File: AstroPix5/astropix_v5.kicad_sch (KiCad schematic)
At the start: 40 parts, among them J1 HBOut, J12 Measures_Analog, J14 Bias, J2 Conn_01x05, J3 pcie_GECCO, J4 HBOut, J5 HBOut, J7 HV_in_external, J8 Conn_01x03, U2 AstroPix5_split_powerring

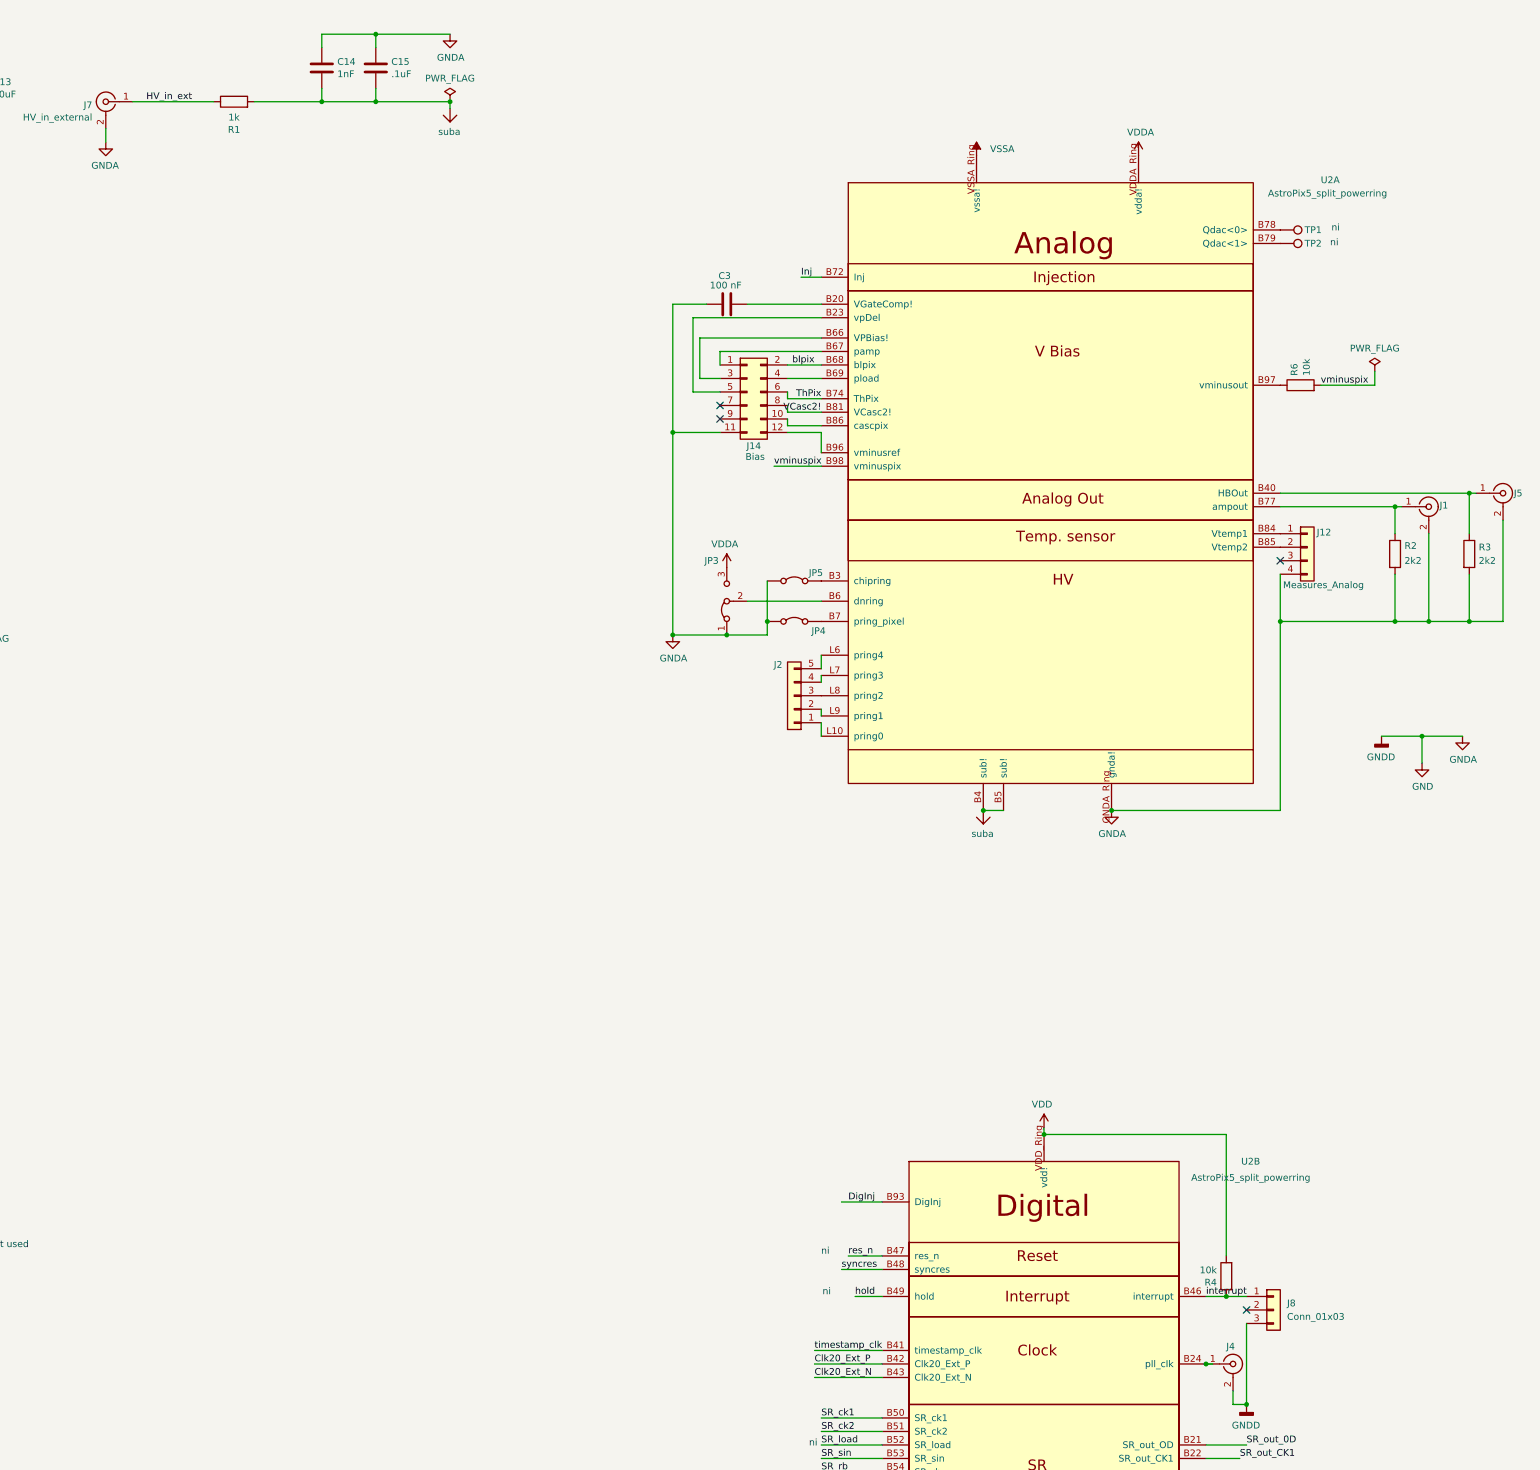
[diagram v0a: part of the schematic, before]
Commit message: Address PCB review comments: add stitching capacitors and increase track spacing
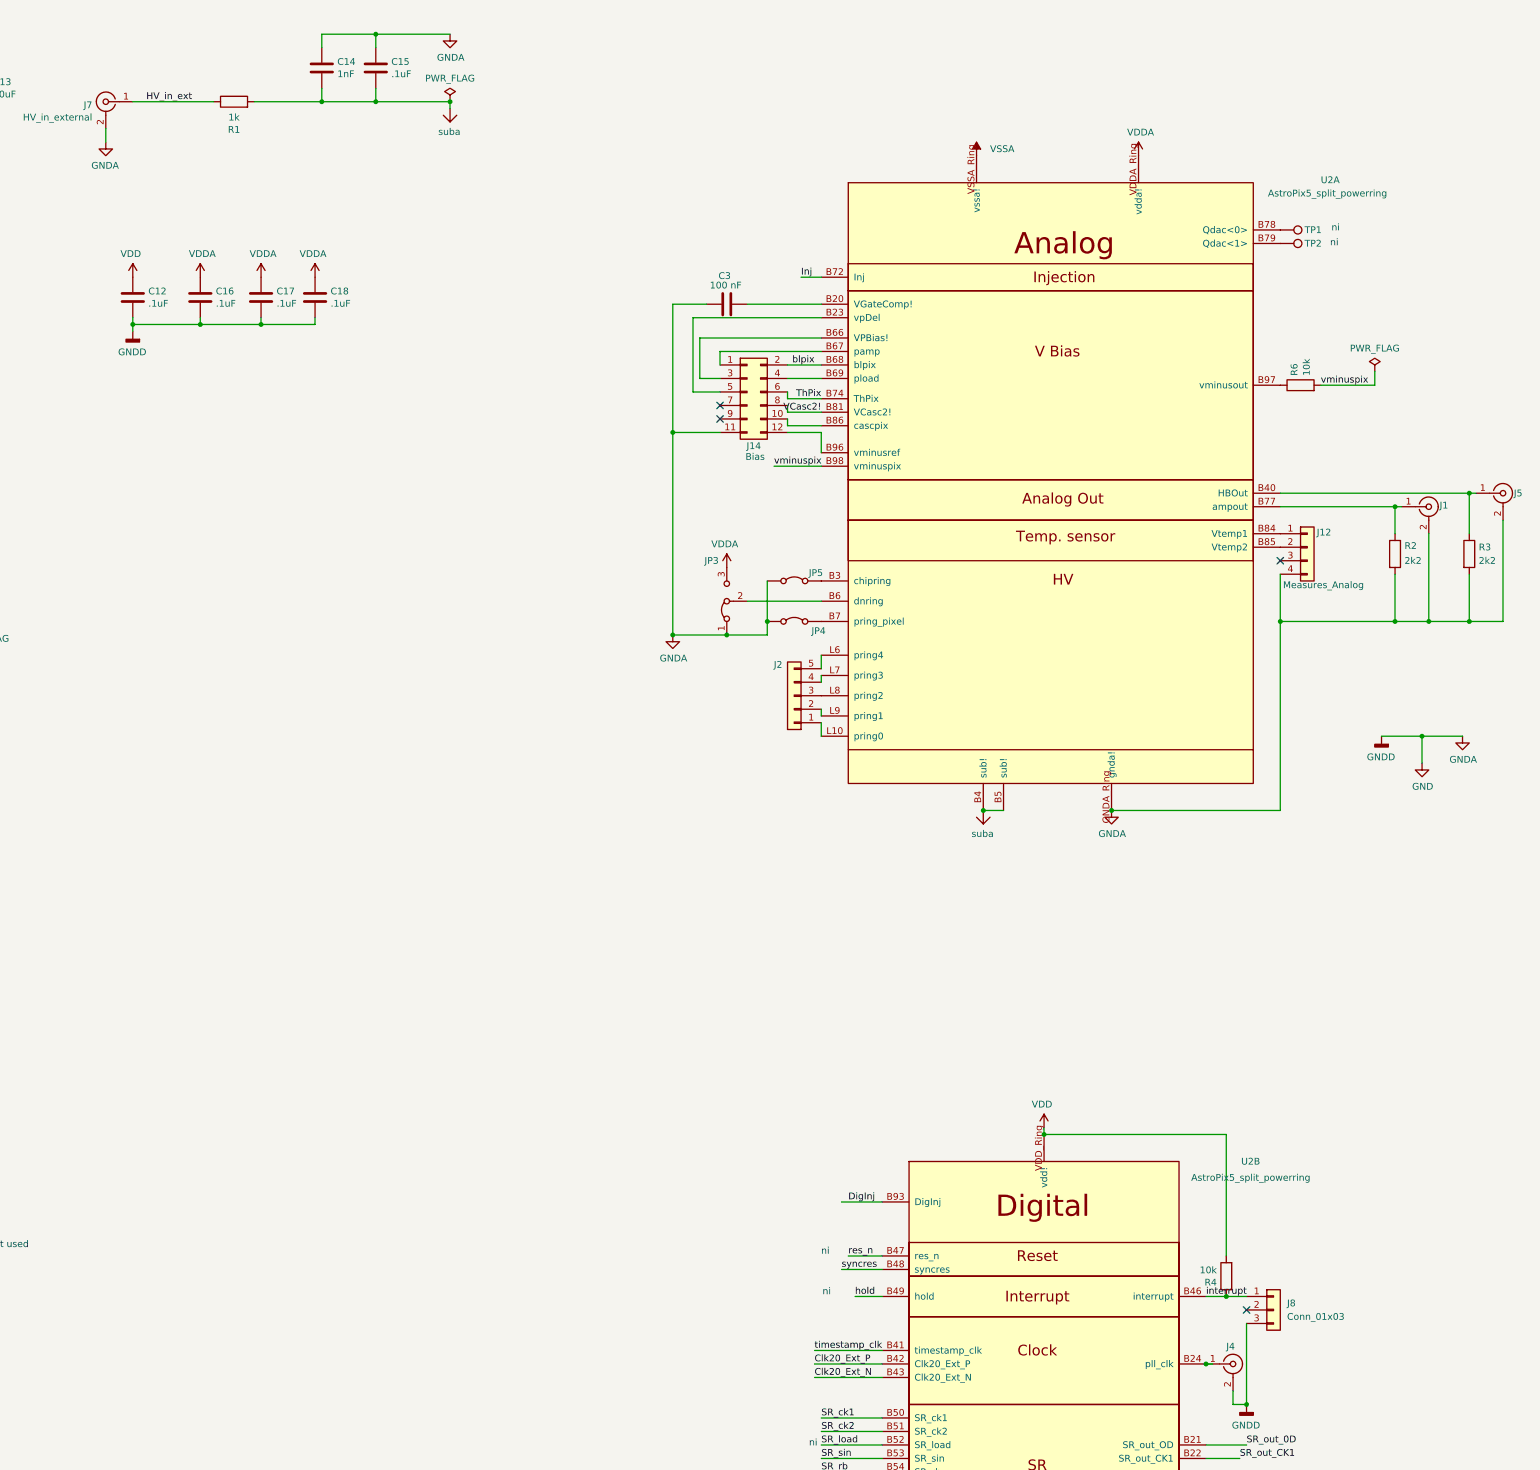
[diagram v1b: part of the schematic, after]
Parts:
- added C12, C16, C17, C18: .1uF, Capacitor_SMD:C_0603_1608Metric, symbol Device:C
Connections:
- net GND: now also C12.2, C16.2, C17.2, C18.2
- net VDD: now also C12.1
- net VDDA: now also C16.1, C17.1, C18.1
